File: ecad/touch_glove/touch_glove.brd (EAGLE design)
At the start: 78.3 x 40.6 mm, 175 parts, among them Q1 MCH3474 4A/30V, Q2 MCH3474 4A/30V, Q3 MCH3474 4A/30V, Q4 MCH3474 4A/30V, Q5 MCH3474 4A/30V, Q6 MCH3474 4A/30V, SW1 4A/28V, Y1 16 MHz

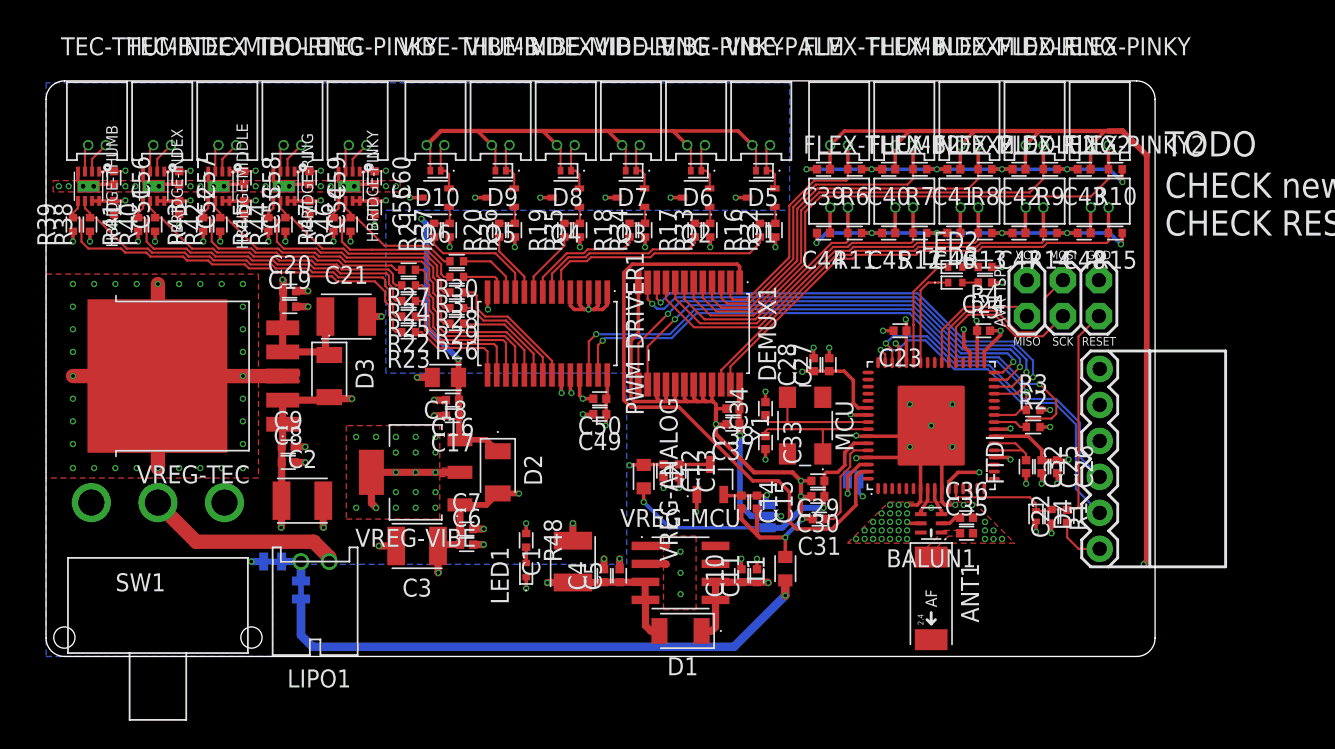
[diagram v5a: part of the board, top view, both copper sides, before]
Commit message: Rev 2: Touch Glove.  Add op amps to flex sensor set 2.
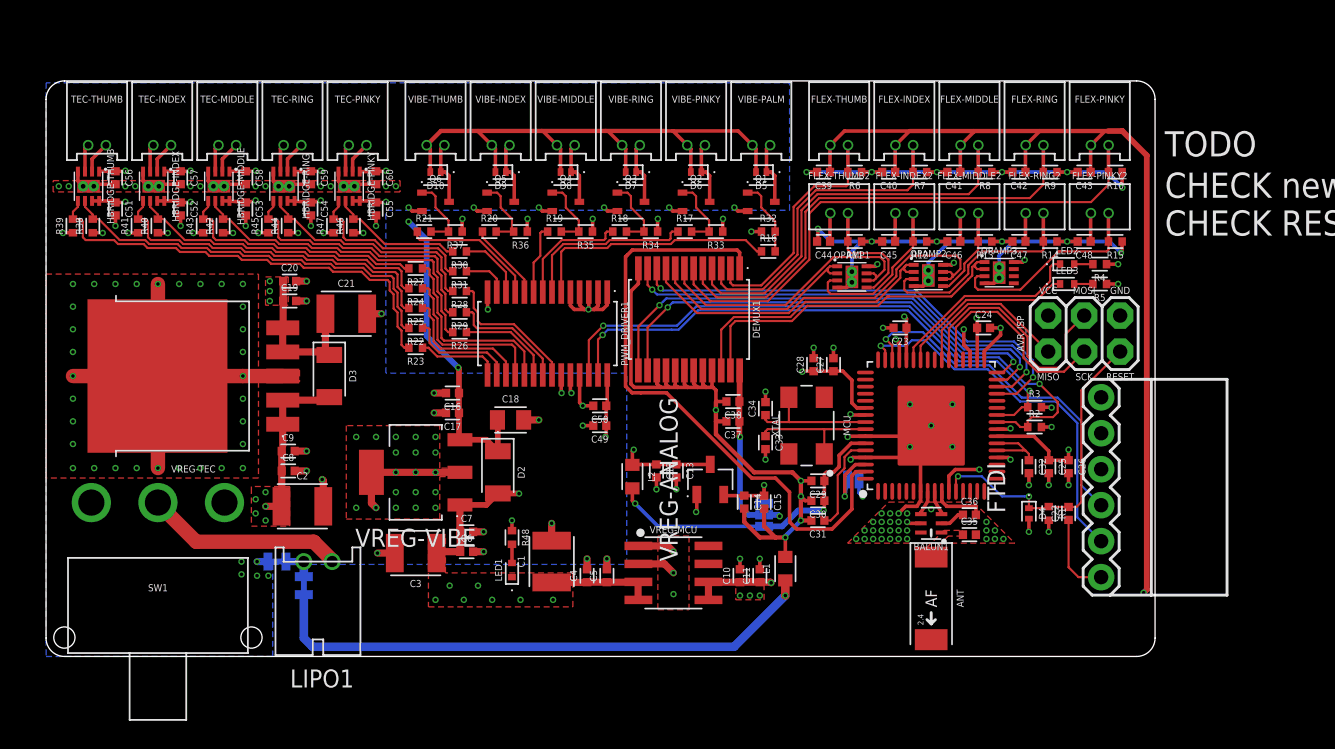
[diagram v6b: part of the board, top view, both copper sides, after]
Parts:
- removed D1: 1A/50V, PiB_discrete_semiconductors:SODFL3516X170
- removed Y1: 16 MHz, PiB:OSCCC500X320X110
- added OPAMP1, OPAMP2, OPAMP3: LM358_DFN-EP, PiB_op_amps:WSON-8-PPAD
- added XTAL: 16 MHz, PiB:OSCCC500X320X110
- C1, C2, C21, C3: value 100uF/16V -> 100uF/10V
- LED1, LED2, LED3: device PiB_leds:LEDC1005X40 -> PiB_leds:LEDC1005X40_LED-0402
- R1, R32, R33, R34, R35, R36, R37, R38, R39, R40, R41, R42, R43, R44, R45, R46, R47, R48: value 10KΩ -> 10K; device PiB_resistors:RESC1005X35 -> PiB_resistors:RESC1005X35_SMD-0402
- R10, R11, R12, R13, R14, R15, R6, R7, R8, R9: value 47K -> 10K; device PiB_resistors:RESC1005X35 -> PiB_resistors:RESC1005X35_SMD-0402
- R16, R17, R18, R19, R2, R20, R21, R22, R23, R24, R25, R26, R27, R28, R29, R3, R30, R31, R4, R5: device PiB_resistors:RESC1005X35 -> PiB_resistors:RESC1005X35_SMD-0402
- moved R4 8.10 mm to (74.4, 27.7)
- moved R5 8.10 mm to (74.4, 26.3)
- moved LED2 7.90 mm to (72.1, 27.7)
- moved LED3 7.90 mm to (72.1, 26.3)
- moved C18 5.49 mm to (32.8, 16.7), turned to 0 degrees
- moved AVR_ISP 2.92 mm to (73.3, 22.8)
- moved FTDI 2.00 mm to (74.5, 12.0)
- moved R16 1.62 mm to (51.0, 28.6), turned to 0 degrees
- moved C1 1.50 mm to (35.7, 6.70)
- moved R23 1.21 mm to (26.1, 21.8)
- moved C4 1.20 mm to (38.2, 5.70)
- moved R48 1.02 mm to (32.9, 8.40)
- moved DEMUX1 1.00 mm to (45.4, 23.8)
- moved LED1 1.00 mm to (32.9, 6.10)
- moved R22 0.94 mm to (26.1, 23.2)
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- renumbered ANT1 to ANT
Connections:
- net A0 renamed SIG
- net PB6 renamed LED_RX
- net PB7 renamed LED_TX
- net PD4 renamed S0
- net PD5 renamed S1
- net PD6 renamed S3
- net PD7 renamed S2
- removed net A1: MCU.64
- removed net A2: MCU.1
- removed net A3: MCU.2
- removed net A4: MCU.3
- removed net A5: MCU.4
- removed net A6: MCU.5
- removed net A7: MCU.6
- removed net PB4: MCU.40
- removed net PB5: MCU.41
- removed net PE2: MCU.48
- removed net PE3: MCU.49
- removed net PE4: MCU.50
- removed net PE5: MCU.51
- removed net PE6: MCU.52
- removed net PE7: MCU.53
- removed net PG0: MCU.14
- removed net PG1: MCU.15
- removed net PG2: MCU.16
- removed net PG3: MCU.17
- removed net PG4: MCU.18
- removed net PG5: MCU.19
- removed net RX1: MCU.27
- removed net SSN: MCU.36
- removed net TX1: MCU.28
- removed net VBATT: C1.1, C2.1, C3.1, C4.1, C5.1, C6.1, C7.1, C8.1, C9.1, D1.K, D2.K, D3.K, LED1.A, SW1.S1, VREG-MCU.3, VREG-MCU.4, VREG-TEC.1, VREG-TEC.2, VREG-VIBE.1
- new net N$10001: FLEX-PINKY2.2, OPAMP3.3, R15.2
- new net N$1004: FLEX-THUMB2.2, OPAMP1.5, R11.2
- new net N$38: FLEX-INDEX2.2, OPAMP1.3, R12.2
- new net N$41: FLEX-RING2.2, OPAMP2.3, R14.2
- new net N$991: FLEX-MIDDLE2.2, OPAMP2.5, R13.2
- new net VBAT: C1.1, C2.1, C3.1, C4.1, C5.1, C6.1, C7.1, C8.1, C9.1, D2.K, D3.K, LED1.A, SW1.S1, VREG-MCU.3, VREG-MCU.4, VREG-TEC.1, VREG-TEC.2, VREG-VIBE.1
- net AGND: now also OPAMP1.4, OPAMP1.GND, OPAMP1.P$1, OPAMP1.P$2, OPAMP2.4, OPAMP2.GND, OPAMP2.P$1, OPAMP2.P$2, OPAMP3.4, OPAMP3.GND, OPAMP3.P$1, OPAMP3.P$2
- net FLEX-INDEX2: now also OPAMP1.1, OPAMP1.2; no longer FLEX-INDEX2.2, R12.2
- net FLEX-MIDDLE2: now also OPAMP2.6, OPAMP2.7; no longer FLEX-MIDDLE2.2, R13.2
- net FLEX-PINKY2: now also OPAMP3.1, OPAMP3.2; no longer FLEX-PINKY2.2, R15.2
- net FLEX-RING2: now also OPAMP2.1, OPAMP2.2; no longer FLEX-RING2.2, R14.2
- net FLEX-THUMB2: now also OPAMP1.6, OPAMP1.7; no longer FLEX-THUMB2.2, R11.2
- net N$15: now also Q2.3; no longer Q2.2
- net N$17: now also Q1.3; no longer Q1.2
- net N$2: now also Q4.3; no longer Q4.2
- net N$3: now also Q5.3; no longer Q5.2
- net N$30: now also Q6.3; no longer Q6.2
- net N$35: now also XTAL.3; no longer Y1.3
- net N$36: now also XTAL.1; no longer Y1.1
- net N$4: now also Q3.3; no longer Q3.2
- net NGND: now also Q1.2, Q2.2, Q3.2, Q4.2, Q5.2, Q6.2; no longer Q1.3, Q2.3, Q3.3, Q4.3, Q5.3, Q6.3
- net VCC: no longer D1.A
- net VSENSOR: now also OPAMP1.8, OPAMP2.8, OPAMP3.8
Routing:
- net VBATT: track 36.9 -> 0.00 mm, vias 6 -> 0
- net VBAT: track 0.00 -> 29.0 mm, vias 0 -> 13
- net VSENSOR: track 157.4 -> 178.9 mm, vias 4 -> 7
- net AGND: track 210.0 -> 227.7 mm, vias 54 -> 48
- net N$41: track 0.00 -> 15.4 mm
- net N$10001: track 0.00 -> 14.6 mm
- net N$38: track 0.00 -> 11.5 mm
- net FLEX-RING2: track 29.9 -> 19.8 mm
- net FLEX-PINKY2: track 34.0 -> 24.5 mm
- net N$1004: track 0.00 -> 8.65 mm
- net FLEX-INDEX2: track 23.4 -> 15.4 mm
- net N$991: track 0.00 -> 6.42 mm
- net LED_TX: track 8.18 -> 14.3 mm
- net LED_RX: track 7.28 -> 12.6 mm
- net GND: track 62.2 -> 66.1 mm
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- added copper zone on layer 1, net 1.8V
- added copper zone on layer 1, net VBAT
- added copper zone on layer 2, net VBAT
- added copper zone on layer 1, net VCC
- removed copper zone on layer 2, net VBATT

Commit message: Replaced supply devices from a non-existent library.
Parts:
- JP1: value JUMPER-SMT_3_NO_SILK -> JUMPER_SMD_3-PAD_NO_NO-SILK; device PiB_connectors:SMT-JUMPER_3_NO_SILK -> PiB_connectors:SMT-JUMPER_3_NO_NO-SILK
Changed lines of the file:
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@@
 <layer number="14" name="Route14" color="1" fill="6" visible="no" active="no"/>
 <layer number="15" name="Route15" color="1" fill="6" visible="yes" active="yes"/>
-<layer number="16" name="Bottom" color="1" fill="1" visible="no" active="yes"/>
+<layer number="16" name="Bottom" color="1" fill="1" visible="yes" active="yes"/>
 <layer number="17" name="Pads" color="2" fill="1" visible="yes" active="yes"/>
 <layer number="18" name="Vias" color="2" fill="1" visible="yes" active="yes"/>
@@
 </layers>
 <board>
-<fusionsync huburn="a.cGVyc29uYWw6dWUyOTIwMzJm" projecturn="a.cGVyc29uYWw6dWUyOTIwMzJmIzIwMTYwNDI5MzA4MDY3NTY" f3durn="urn:adsk.wipprod:dm.lineage:dZKVV2TOQ-GfPmiZokfcDw" pcbguid="55b963d9-4c6d-479b-bd22-0a896272d867" lastpulledtime="" lastsyncedchangeguid="f1565c9e-5985-66dc-efcc-659af679d701"/>
+<fusionsync huburn="a.cGVyc29uYWw6dWUyOTIwMzJm" projecturn="a.cGVyc29uYWw6dWUyOTIwMzJmIzIwMTgwNTE1MTMyMDQwMDA2" f3durn="urn:adsk.wipprod:dm.lineage:LtZLZUV9QYivw_cdolU7_g" pcbguid="6a75e65d-6c45-496d-a9c6-e14d0e7ecd70" lastpulledtime="" lastsyncedchangeguid="654cb818-a030-a7ac-f8e4-36d8fb917082"/>
 <plain>
 <wire x1="77.0072" y1="40.64" x2="1.3008" y2="40.64" width="0" layer="20"/>
@@
 <element name="U$1" library="PiB_logo" package="LRG-LOGO-2" value="" x="29" y="7" rot="MR0"/>
 <element name="U$2" library="PiB_logo" package="MRSWIRLYEYES-LOGO" value="" x="43" y="8" rot="MR0"/>
-<element name="JP1" library="PiB_connectors" library_urn="urn:adsk.eagle:library:2993000" package="SMT-JUMPER_3_NO_SILK" package3d_urn="urn:adsk.eagle:package:2993085/1" value="JUMPER-SMT_3_NO_SILK" x="50.7" y="10" rot="MR270"/>
+<element name="JP1" library="PiB_connectors" package="SMT-JUMPER_3_NO_NO-SILK" value="JUMPER_SMD_3-PAD_NO_NO-SILK" x="50.7" y="10" rot="MR270"/>
 <element name="JP2" library="PiB_connectors" package="SMT-JUMPER_2_NO_SILK" value="JUMPER-SMT_2_NO_SILK" x="57" y="12.5" rot="MR0"/>
 <element name="OPAMP1" library="PiB_op_amps" package="WSON-8-PPAD" package3d_urn="urn:adsk.eagle:package:2992818/3" value="LM358_DFN-EP" x="56.9" y="26.8"/>
@@
 <contactref element="C50" pad="1"/>
 <contactref element="C49" pad="1"/>
-<contactref element="R1" pad="2"/>
-<contactref element="D4" pad="K"/>
 <contactref element="C11" pad="1"/>
 <contactref element="C10" pad="1"/>
@@
 <wire x1="65.7425" y1="23.8575" x2="65.7" y2="23.9" width="0.254" layer="1"/>
 <via x="65.7" y="23.9" extent="1-16" drill="0.254"/>
-<wire x1="69.4" y1="9.7299" x2="69.4" y2="8.8" width="0.254" layer="1"/>
-<via x="69.4" y="8.8" extent="1-16" drill="0.254"/>
-<wire x1="70.8" y1="9.6175" x2="70.8" y2="8.8" width="0.254" layer="1"/>
-<via x="70.8" y="8.8" extent="1-16" drill="0.254"/>
 <wire x1="57.8553" y1="17.55" x2="57.25" y2="17.55" width="0.254" layer="1"/>
 <wire x1="57.25" y1="17.55" x2="56.9" y2="17.9" width="0.254" layer="1"/>
@@
 <wire x1="70.96771875" y1="17.6" x2="71" y2="17.56771875" width="0.254" layer="1"/>
 <via x="71" y="17.56771875" extent="1-16" drill="0.254"/>
+<contactref element="R1" pad="2"/>
+<contactref element="D4" pad="K"/>
+<wire x1="69.4" y1="9.7299" x2="69.4" y2="8.8" width="0.254" layer="1"/>
+<via x="69.4" y="8.8" extent="1-16" drill="0.254"/>
+<wire x1="70.8" y1="9.6175" x2="70.8" y2="8.8" width="0.254" layer="1"/>
+<via x="70.8" y="8.8" extent="1-16" drill="0.254"/>
 </signal>
 <signal name="FLEX-RING1">
@@
 <wire x1="70.3" y1="28.6" x2="66.0951375" y2="28.6" width="0.1524" layer="1"/>
 <wire x1="66.0951375" y1="28.6" x2="65.1206" y2="27.6254625" width="0.1524" layer="1"/>
-<wire x1="65.1206" y1="27.6254625" x2="65.1206" y2="27.5" width="0.1524" layer="1"/>
-<wire x1="65.1206" y1="27.5" x2="65.1206" y2="27.0206" width="0.1524" layer="1"/>
+<wire x1="65.1206" y1="27.6254625" x2="65.1206" y2="27.0206" width="0.1524" layer="1"/>
 <wire x1="65.1206" y1="27.0206" x2="63.8" y2="25.7" width="0.1524" layer="1"/>
 </signal>
@@
 </signals>
 <mfgpreviewcolors>
-<mfgpreviewcolor name="soldermaskcolor" color="0xC8008000"/>
+<mfgpreviewcolor name="soldermaskcolor" color="0xC855007F"/>
 <mfgpreviewcolor name="silkscreencolor" color="0xFFFEFEFE"/>
 <mfgpreviewcolor name="backgroundcolor" color="0xFF282828"/>
@@
 which will not be processed correctly with this version.
 </note>
-<note version="8.2" severity="warning">
-Since Version 8.2, EAGLE supports online libraries. The ids
-of those online libraries will not be understood (or retained)
-with this version.
-</note>
 <note version="8.3" severity="warning">

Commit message: Rev 2: Touch Glove.  Updated library meta data to reflect item availability.  Add 3D STEP file.
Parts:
- JP2: value JUMPER-SMT_2_NO_SILK -> JUMPER_SMD_2-PAD_NO_SILK
- MCU: value ATMEGA128RFA1_VFQFN-64_NO-EXPOSED-PAD -> ATMEGA128RFA1
- OPAMP1, OPAMP2, OPAMP3: value LM358_DFN-EP -> LM358
- R5: value 2K -> 1K
